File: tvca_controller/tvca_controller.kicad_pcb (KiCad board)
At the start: 2 copper layers, 55 parts, among them J1 Programming Header, J2 PT 1,5/ 4-5,0-H, J3 4DB-P108-02, J4 PT 1,5/ 4-5,0-H, J5 4DB-P108-02, J6 PT 1,5/ 4-5,0-H, J7 4DB-P108-02, J9 4DB-P108-02, U1 PIC18F26K83, U2 MCP2562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

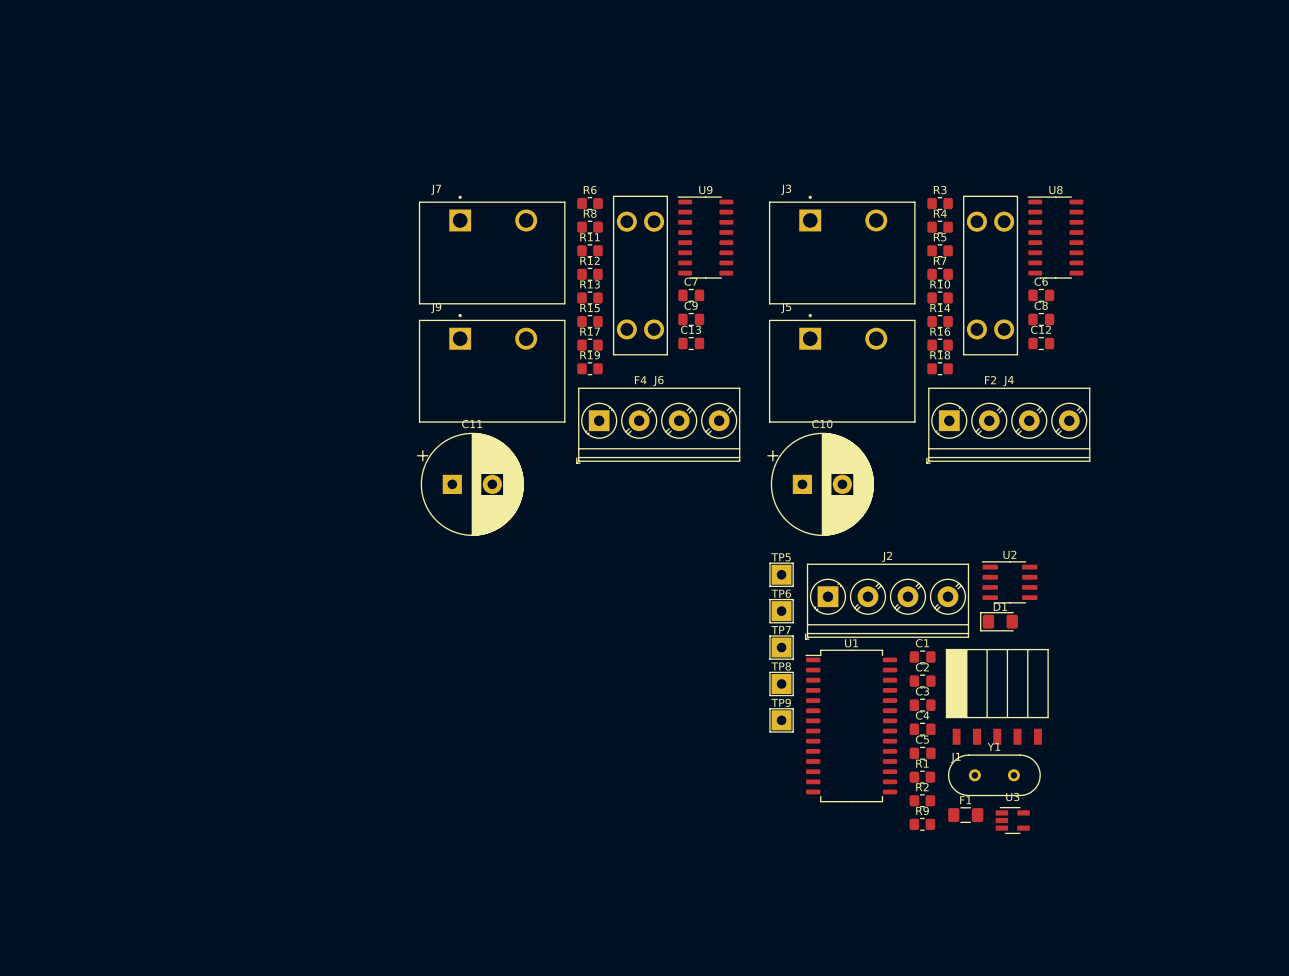
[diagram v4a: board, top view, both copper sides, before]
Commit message: Get started on PCB layout
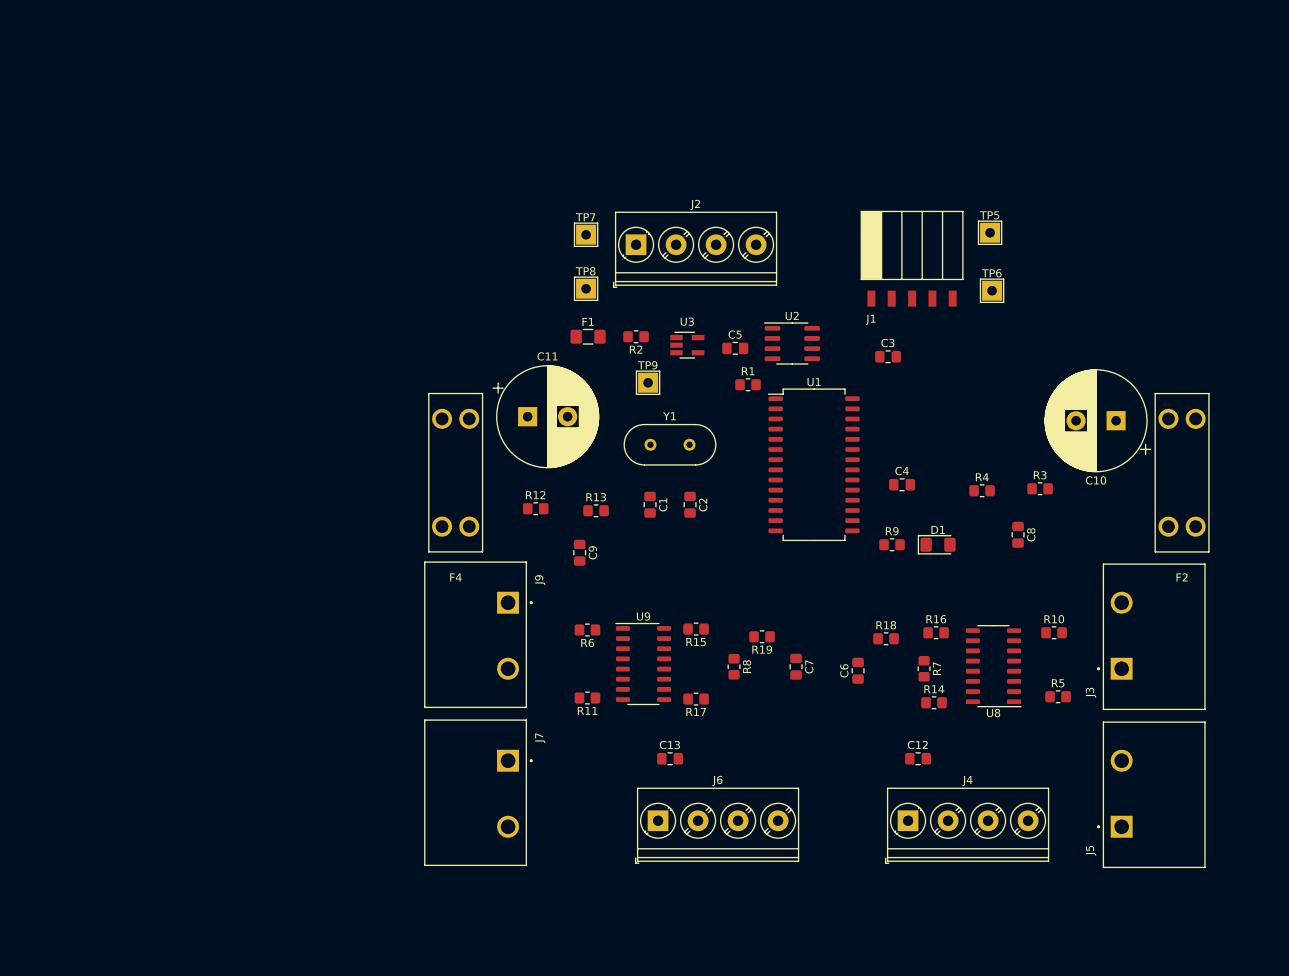
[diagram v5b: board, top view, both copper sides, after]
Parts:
- moved F1 76.2 mm to (118.2, 82.5)
- moved J5 72.4 mm to (185.0, 143.8), turned to 90 degrees
- moved U3 72.0 mm to (130.7, 83.5)
- moved J3 68.2 mm to (185.0, 124.0), turned to 90 degrees
- moved R2 68.2 mm to (124.2, 82.5), turned to 180 degrees
- moved J7 67.8 mm to (108.2, 135.5), turned to -90 degrees
- moved Y1 57.9 mm to (126.0, 96.0)
- moved R8 57.8 mm to (136.5, 123.8), turned to -90 degrees
- moved R5 57.7 mm to (177.0, 127.5)
- moved TP7 57.1 mm to (118.0, 69.8)
- moved R11 55.9 mm to (118.2, 127.7), turned to 180 degrees
- moved J1 55.8 mm to (153.7, 77.7)
- moved C5 55.8 mm to (136.7, 84.0)
- moved TP8 55.1 mm to (118.0, 76.5)
- moved U8 54.1 mm to (168.9, 123.7), turned to 180 degrees
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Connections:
- J5 pad 1: /Motor_1/OUT1 -> /Motor_1/OUT_1
- J5 pad 2: /Motor_1/OUT2 -> /Motor_1/OUT_2
- J7 pad 1: /Motor_2/OUT1 -> /Motor_2/OUT_1
- J7 pad 2: /Motor_2/OUT2 -> /Motor_2/OUT_2

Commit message: Move the pic a bit
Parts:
- moved U1 4.84 mm to (145.9, 103.3)
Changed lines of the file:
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@@
   )
   (footprint "Package_SO:SOIC-28W_7.5x18.7mm_P1.27mm" (layer "F.Cu")
-    (at 146.5 98.5)
+    (at 145.95 103.305)
     (descr "SOIC, 28 Pin (https://www.akm.com/akm/en/file/datasheet/AK5394AVS.pdf#page=23), generated with kicad-footprint-generator ipc_gullwing_generator.py")
     (tags "SOIC SO")

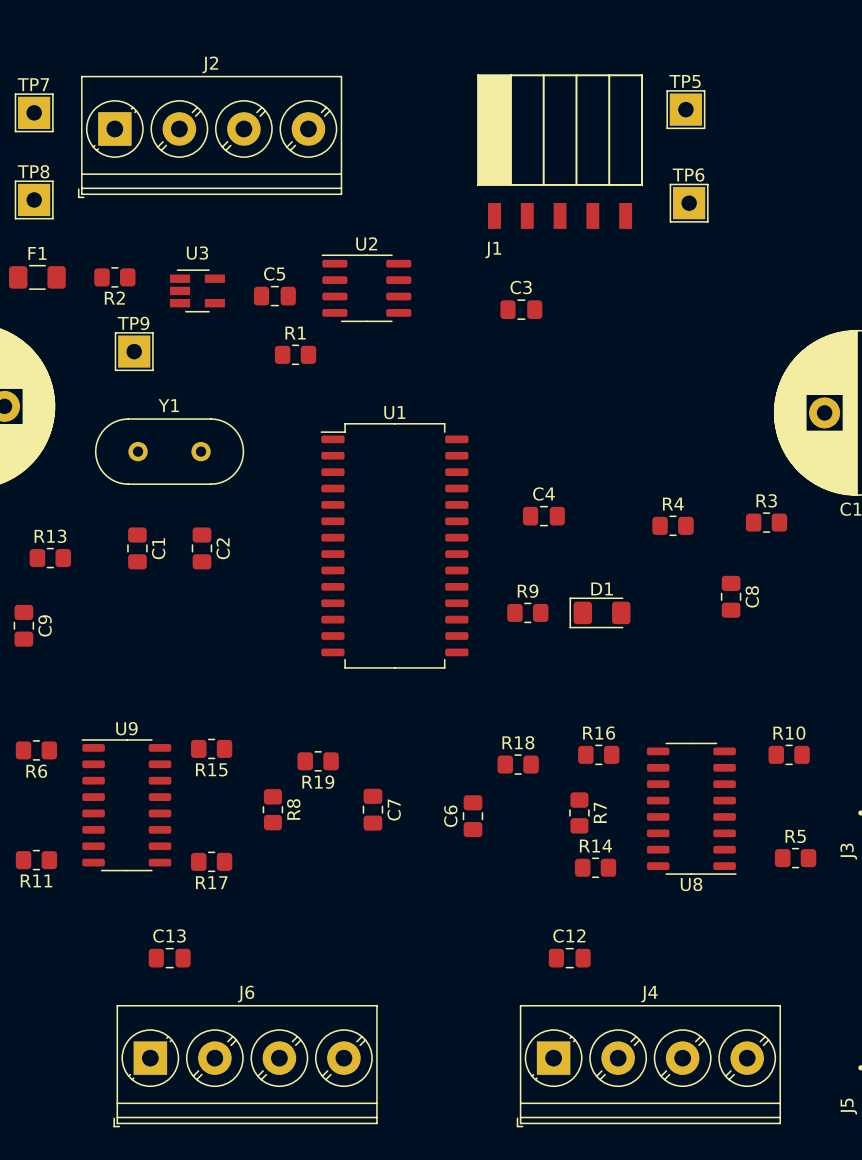
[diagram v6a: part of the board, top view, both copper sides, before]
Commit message: Fix screw terminal
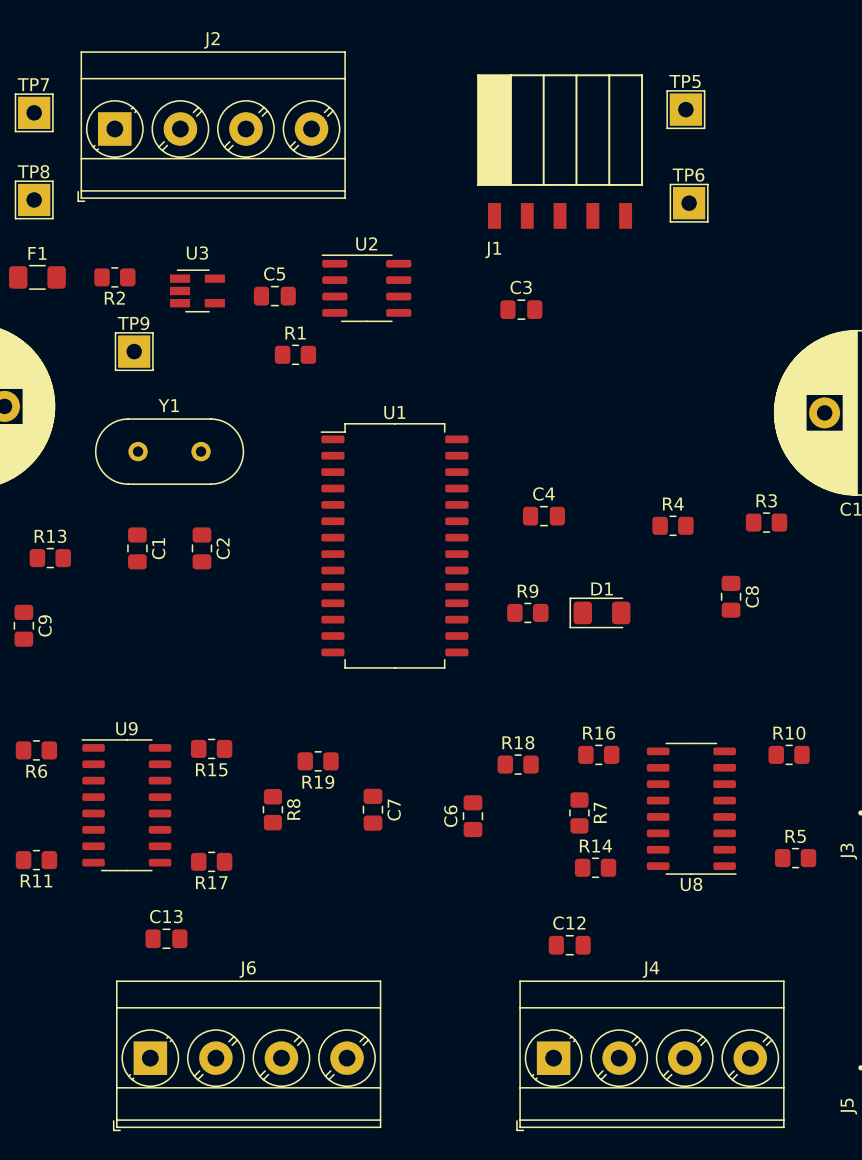
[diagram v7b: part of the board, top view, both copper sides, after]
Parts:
- J2, J4, J6: footprint TerminalBlock_Phoenix:TerminalBlock_Phoenix_PT-1,5-4-5.0-H_1x04_P5.00mm_Horizontal -> TerminalBlock_Phoenix:TerminalBlock_Phoenix_MKDS-3-4-5.08_1x04_P5.08mm_Horizontal
- moved C13 1.52 mm to (128.2, 133.8)
- moved C12 1.00 mm to (159.5, 134.2)

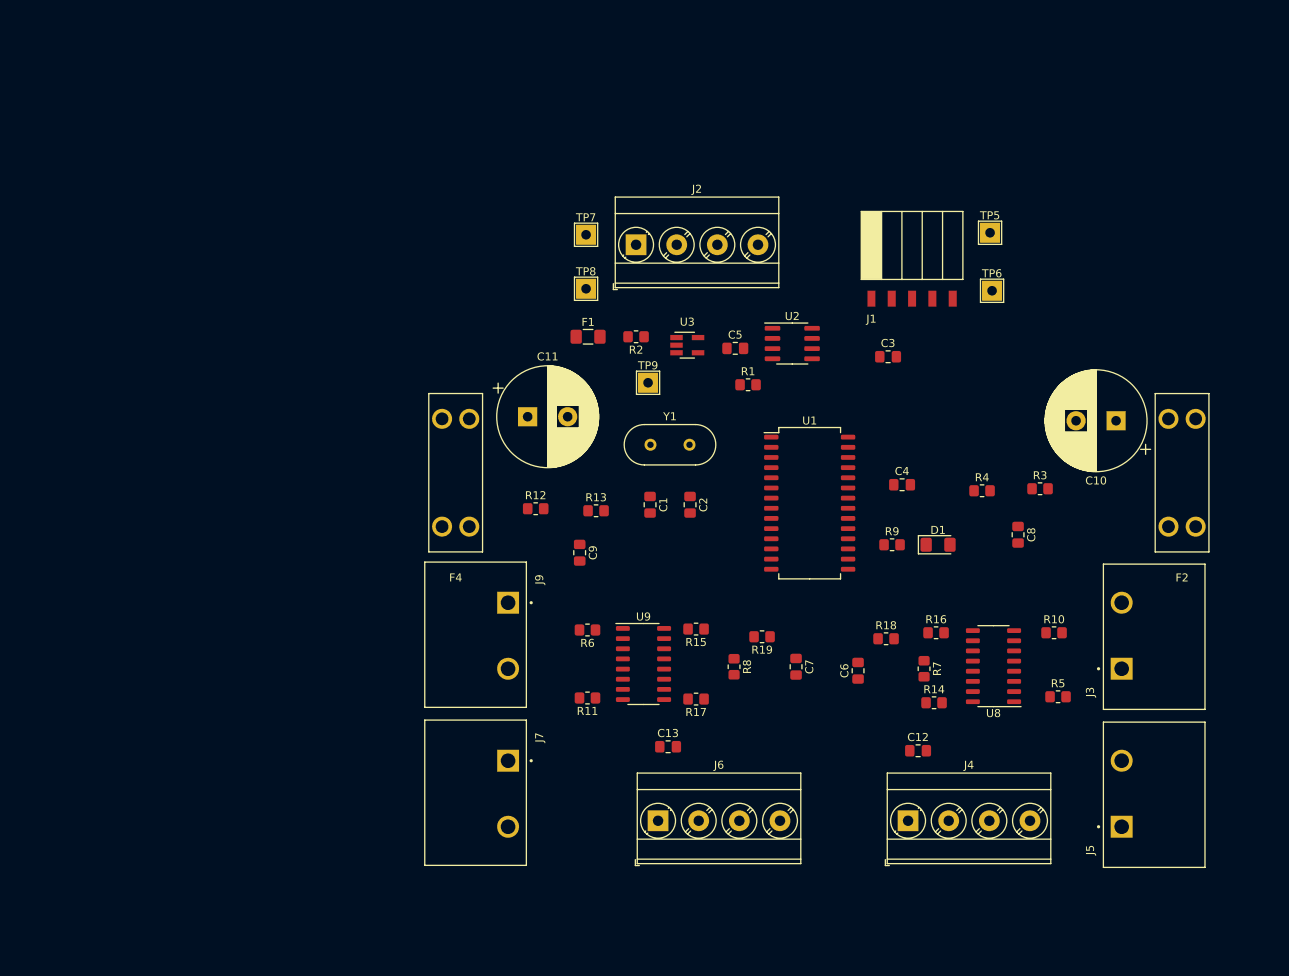
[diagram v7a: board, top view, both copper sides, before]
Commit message: Calculate R sense
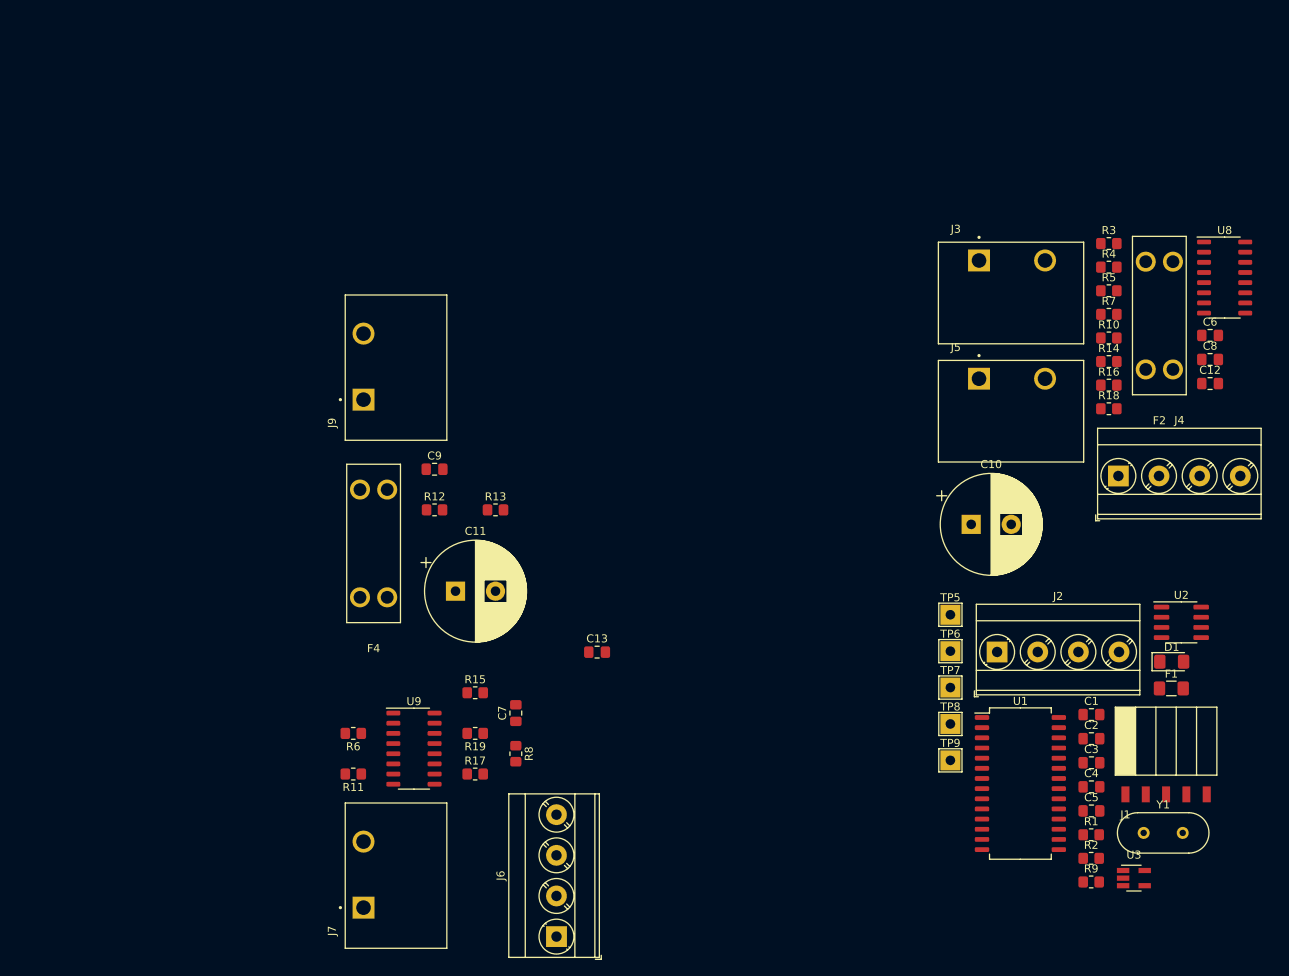
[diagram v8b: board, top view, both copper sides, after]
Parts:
- R7, R8: value R_SENSE -> 400 R
- moved U3 86.9 mm to (186.5, 150.2)
- moved R2 86.5 mm to (181.1, 147.7), turned to 0 degrees
- moved F1 85.1 mm to (191.2, 126.5)
- moved Y1 78.5 mm to (187.7, 144.5)
- moved C5 73.0 mm to (181.2, 141.8)
- moved TP7 72.6 mm to (163.5, 126.3)
- moved TP8 70.9 mm to (163.5, 130.9)
- moved R1 70.7 mm to (181.1, 144.8)
- moved J1 69.6 mm to (185.4, 139.7)
- moved J2 68.0 mm to (169.4, 121.9)
- moved C1 61.1 mm to (181.2, 129.7), turned to 0 degrees
- moved C6 60.8 mm to (196.0, 82.3), turned to 0 degrees
- moved TP9 60.5 mm to (163.5, 135.4)
- moved U2 59.8 mm to (192.4, 118.2)
- moved J5 58.8 mm to (167.1, 87.7), turned to 0 degrees
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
